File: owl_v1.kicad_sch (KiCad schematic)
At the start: 15 parts, among them J1 USB_C_Receptacle_USB2.0_14P, U1 STM32F103C8T6, U2 XC6206P302

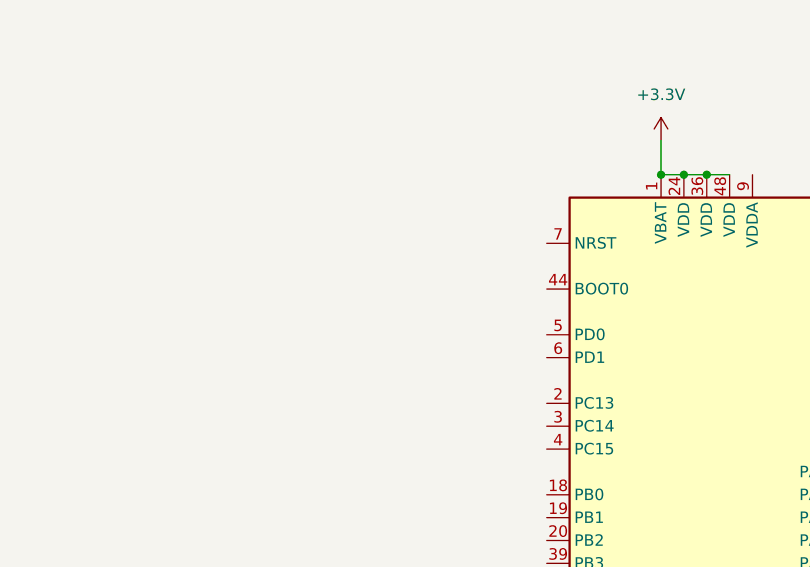
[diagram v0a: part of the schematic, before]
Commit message: [feat] Add boot pin switch
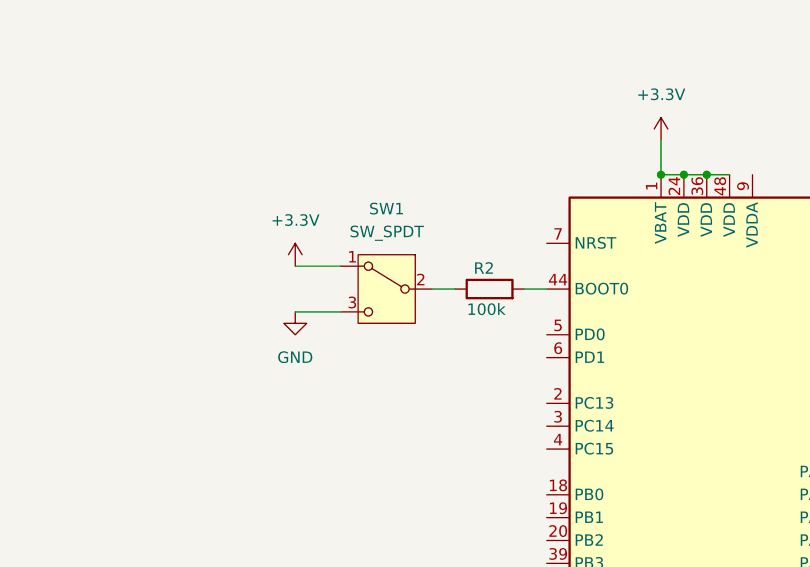
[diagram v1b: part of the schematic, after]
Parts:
- added R2: 100k, symbol Device:R
- added SW1: SW_SPDT, symbol Switch:SW_SPDT
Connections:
- net +3.3V: now also SW1.1 (A)
- net GND: now also SW1.3 (C)
- net at U1.44 (BOOT0): now also R2.2
- new net: R2.1, SW1.2 (B)

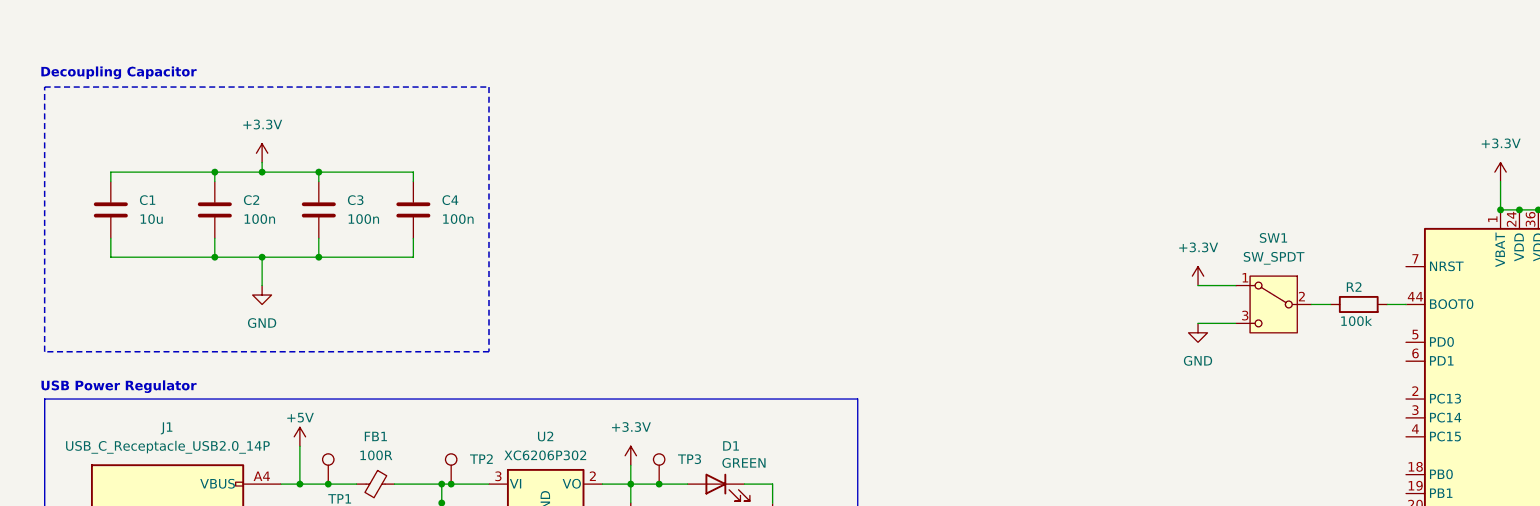
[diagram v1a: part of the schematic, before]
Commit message: [chore] Add comments on why decoupling capacitor is used
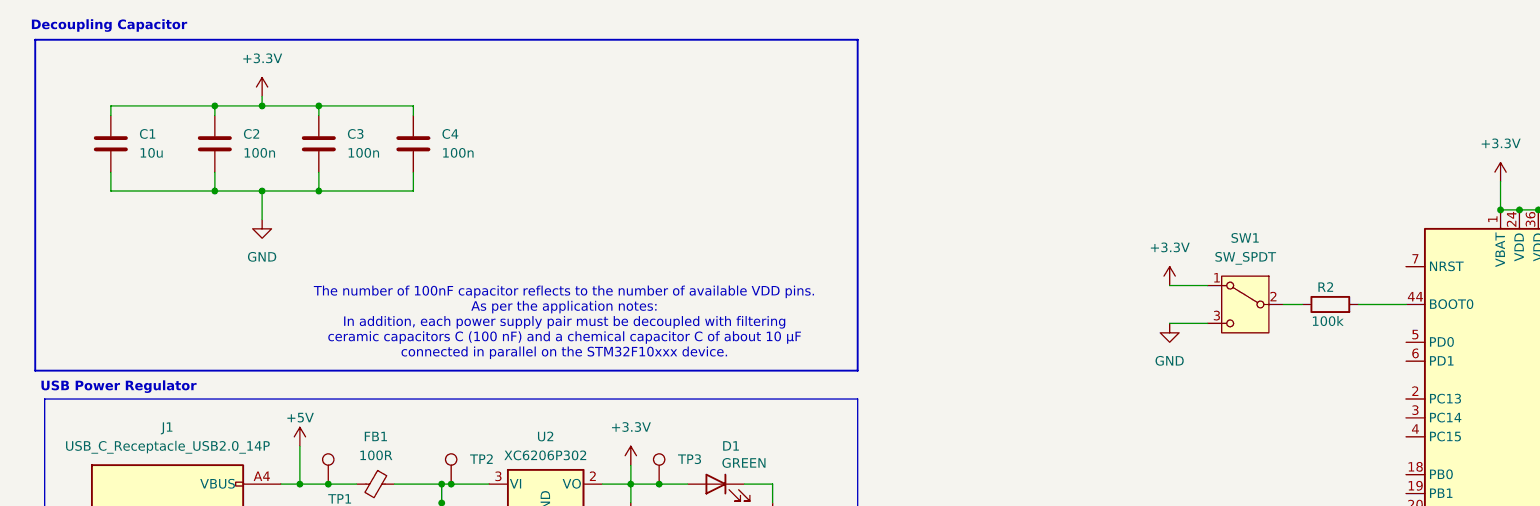
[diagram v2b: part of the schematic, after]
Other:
- note added: "The number of 100nF capacitor reflects to the number of available VDD pins. As per the application notes: In addition, each power supply pair must be decoupled with filtering ceramic capacitors C (100 nF) and a chemical capacitor C of about 10 μF connected in parallel on the STM32F10xxx device."
- moved on the sheet: C1, C2, C3, C4, R2, SW1

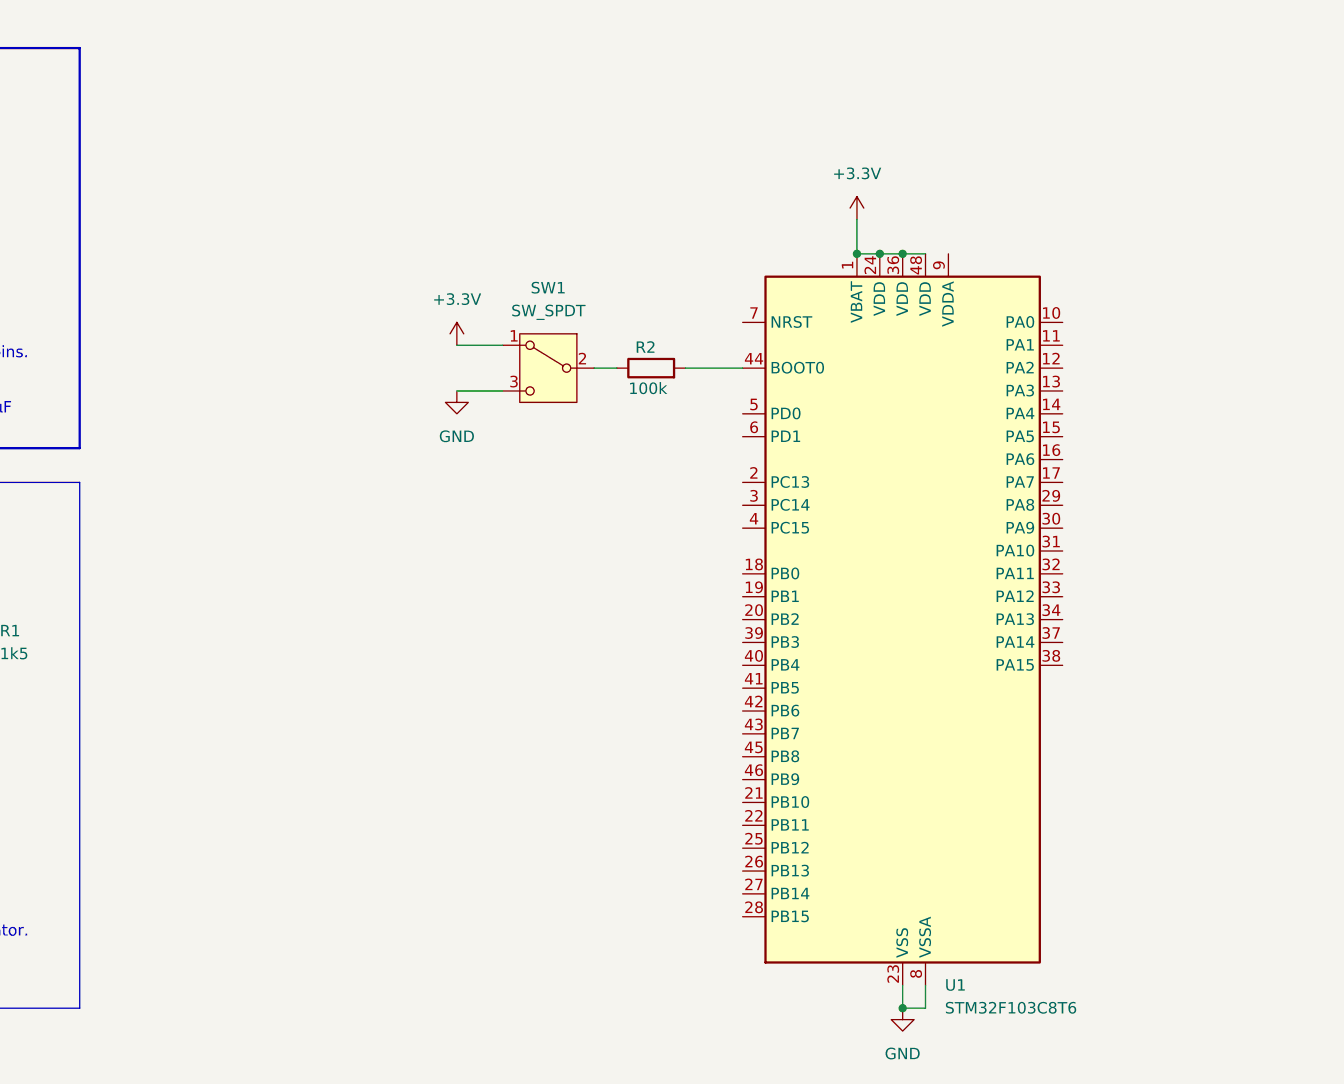
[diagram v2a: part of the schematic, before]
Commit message: [feat] Integrate HSE and LSE crystal, populate global label for SWD
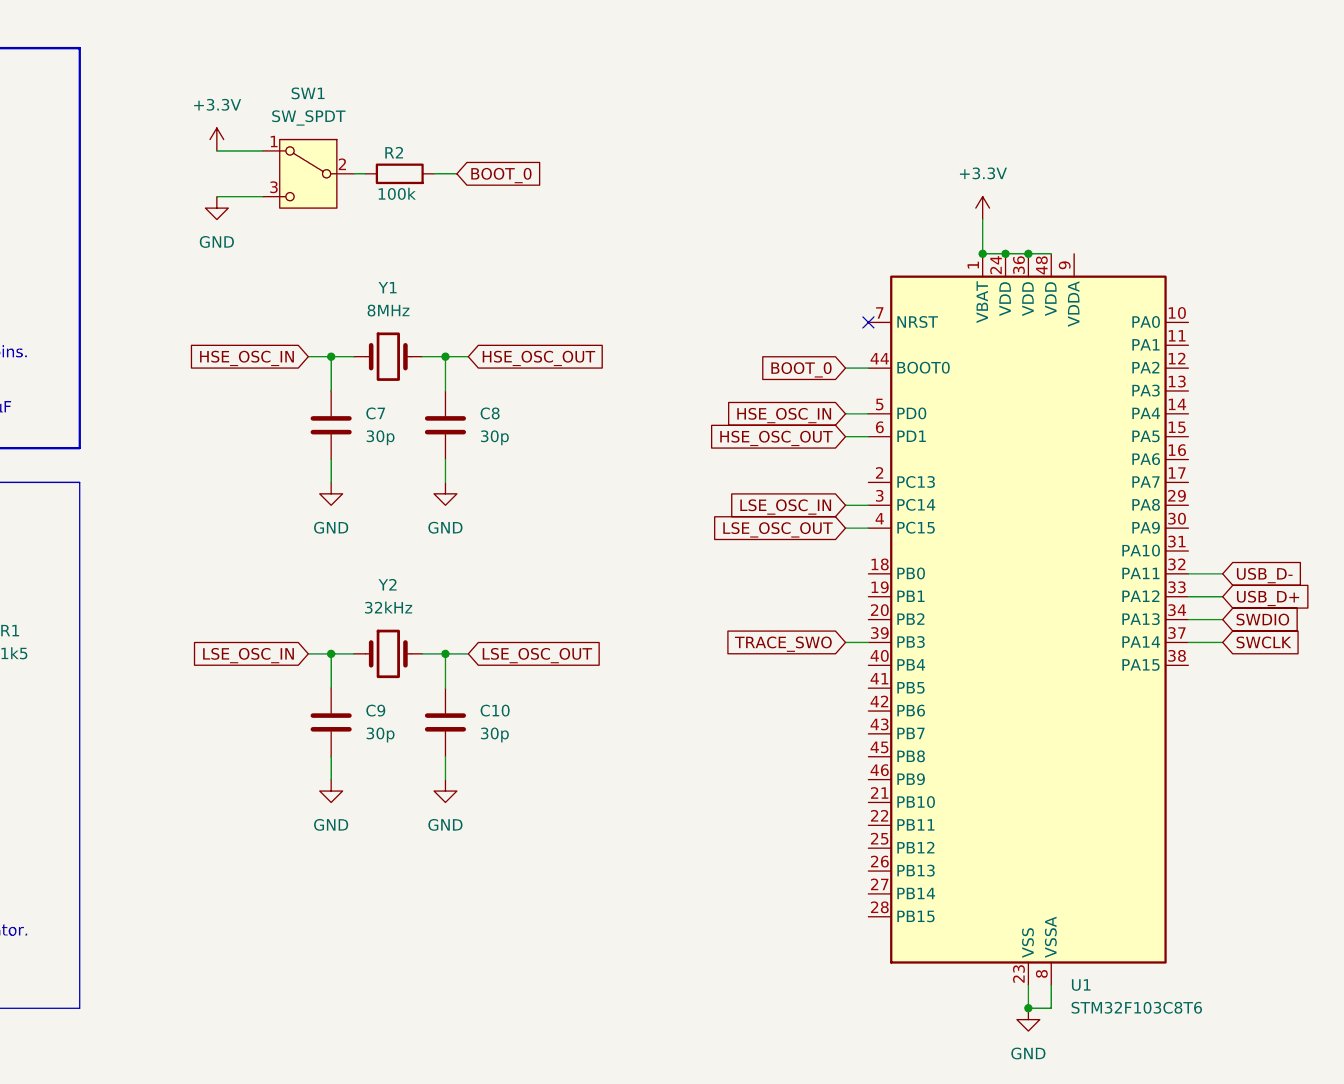
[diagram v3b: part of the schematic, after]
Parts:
- added C10, C7, C8, C9: 30p, Capacitor_SMD:C_0603_1608Metric, symbol Device:C
- added Y1: 8MHz, symbol Device:Crystal
- added Y2: 32kHz, symbol Device:Crystal
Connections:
- net GND: now also C10.2, C7.2, C8.2, C9.2
- net LSE_OSC_IN: now reaches U1.3 (PC14)
- net LSE_OSC_IN: now also C9.1, Y2.1
- net USB_D-: now reaches U1.32 (PA11)
- net USB_D+: now reaches U1.33 (PA12)
- net SWDIO: now reaches U1.34 (PA13)
- net SWCLK: now reaches U1.37 (PA14)
- net TRACE_SWO: now reaches U1.39 (PB3)
- net LSE_OSC_OUT: now reaches U1.4 (PC15)
- net LSE_OSC_OUT: now also C10.1, Y2.2
- net BOOT_0: now reaches R2.2, U1.44 (BOOT0)
- net HSE_OSC_IN: now reaches U1.5 (PD0)
- net HSE_OSC_IN: now also C7.1, Y1.1
- net HSE_OSC_OUT: now reaches U1.6 (PD1)
- net HSE_OSC_OUT: now also C8.1, Y1.2
- no-connect marks 3 -> 4
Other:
- moved on the sheet: U1

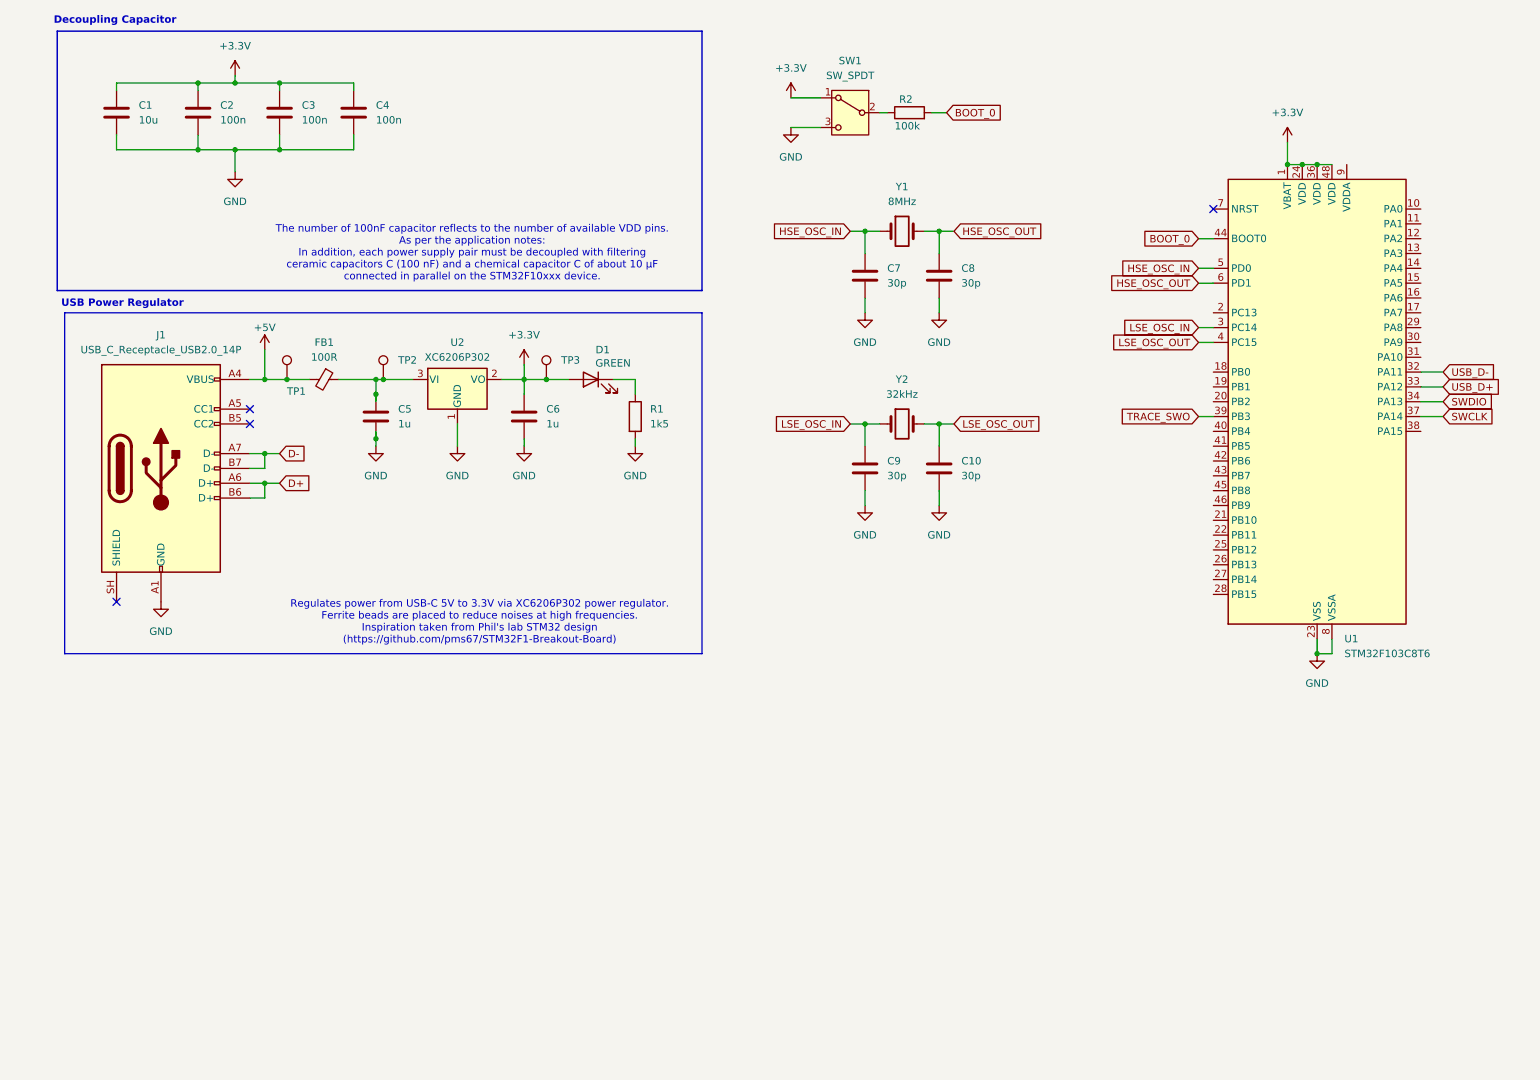
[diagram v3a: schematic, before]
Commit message: [feat] Add HSE and LSE crystals for RCC
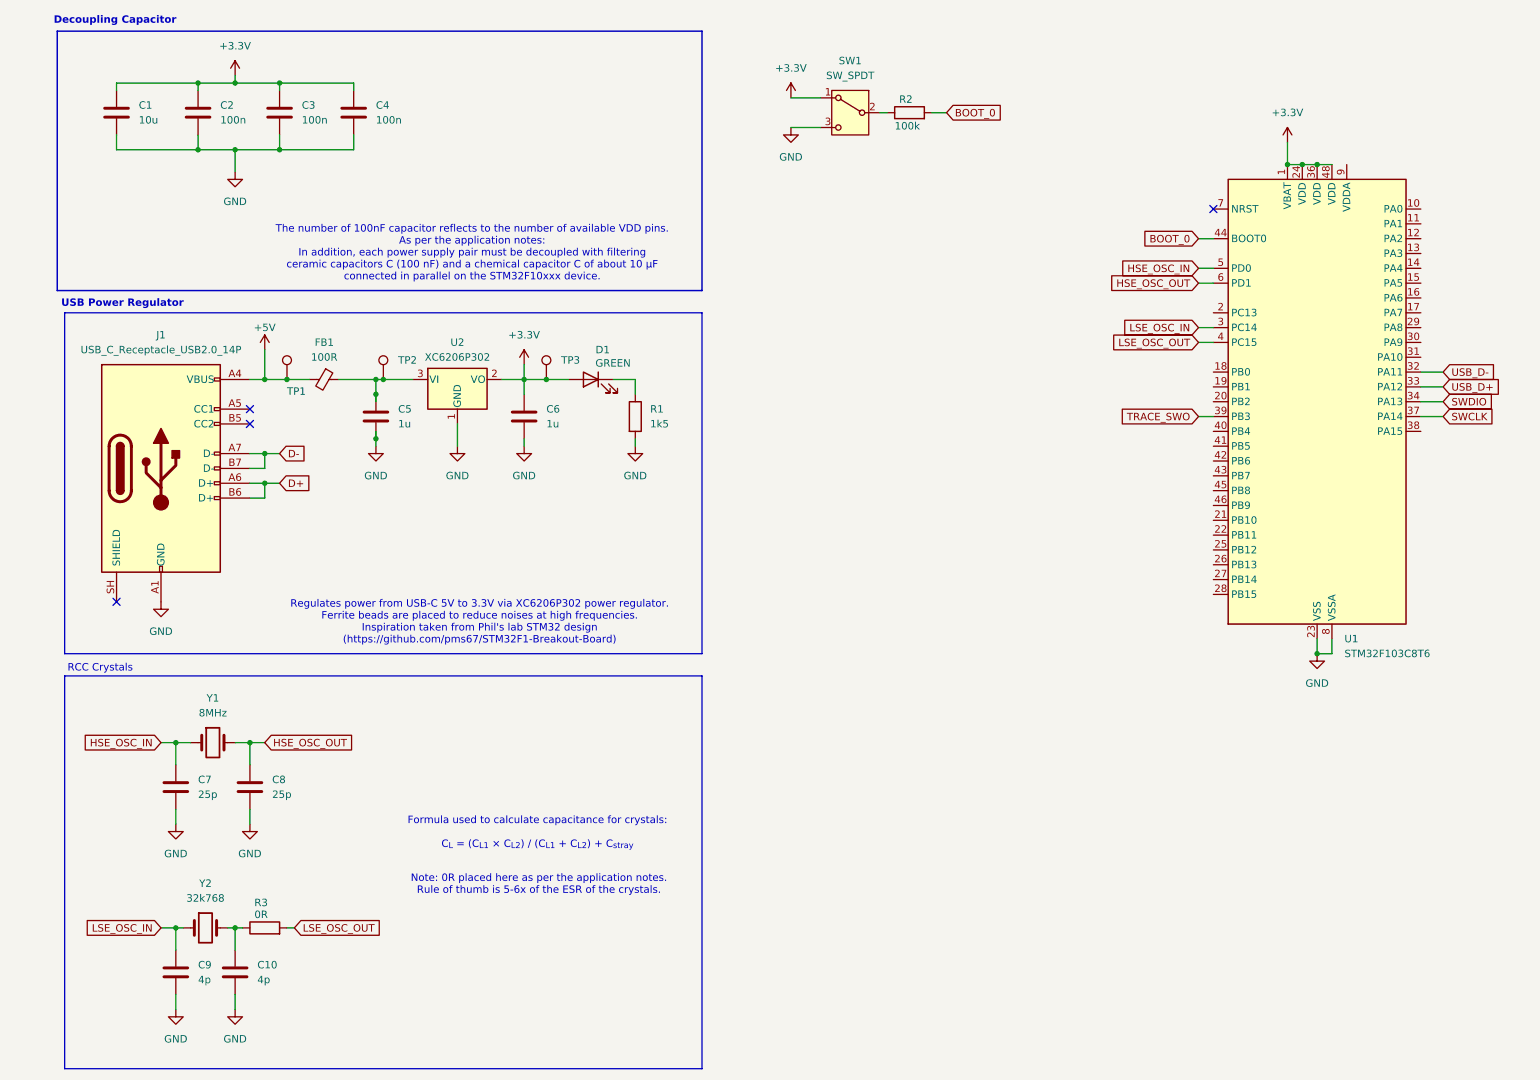
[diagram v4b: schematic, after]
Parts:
- added R3: 0R, Resistor_SMD:R_0603_1608Metric, symbol Device:R
- C10, C9: value 30p -> 4p
- C7, C8: value 30p -> 25p
- Y1: footprint (none) -> Crystal:Crystal_SMD_HC49-SD
- Y2: value 32kHz -> 32k768; footprint (none) -> Crystal:Crystal_SMD_MicroCrystal_CC8V-T1A-2Pin_2.0x1.2mm_HandSoldering
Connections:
- net LSE_OSC_OUT: now also R3.2; no longer C10.1, Y2.2
- new net: C10.1, R3.1, Y2.2
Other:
- note added: "Formula used to calculate capacitance for crystals: C_{L} = (C_{L1} × C_{L2}) / (C_{L1} + C_{L2}) + C_{stray}"
- note added: "Note: 0R placed here as per the application notes. Rule of thumb is 5-6x of the ESR of the crystals."
- note added: "RCC Crystals"
- moved on the sheet: C7, C8, Y1, Y2
